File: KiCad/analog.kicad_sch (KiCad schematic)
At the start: 25 parts, among them J1 Conn_01x02, U1 LM1117T-3.3, U2 LM2596T-5

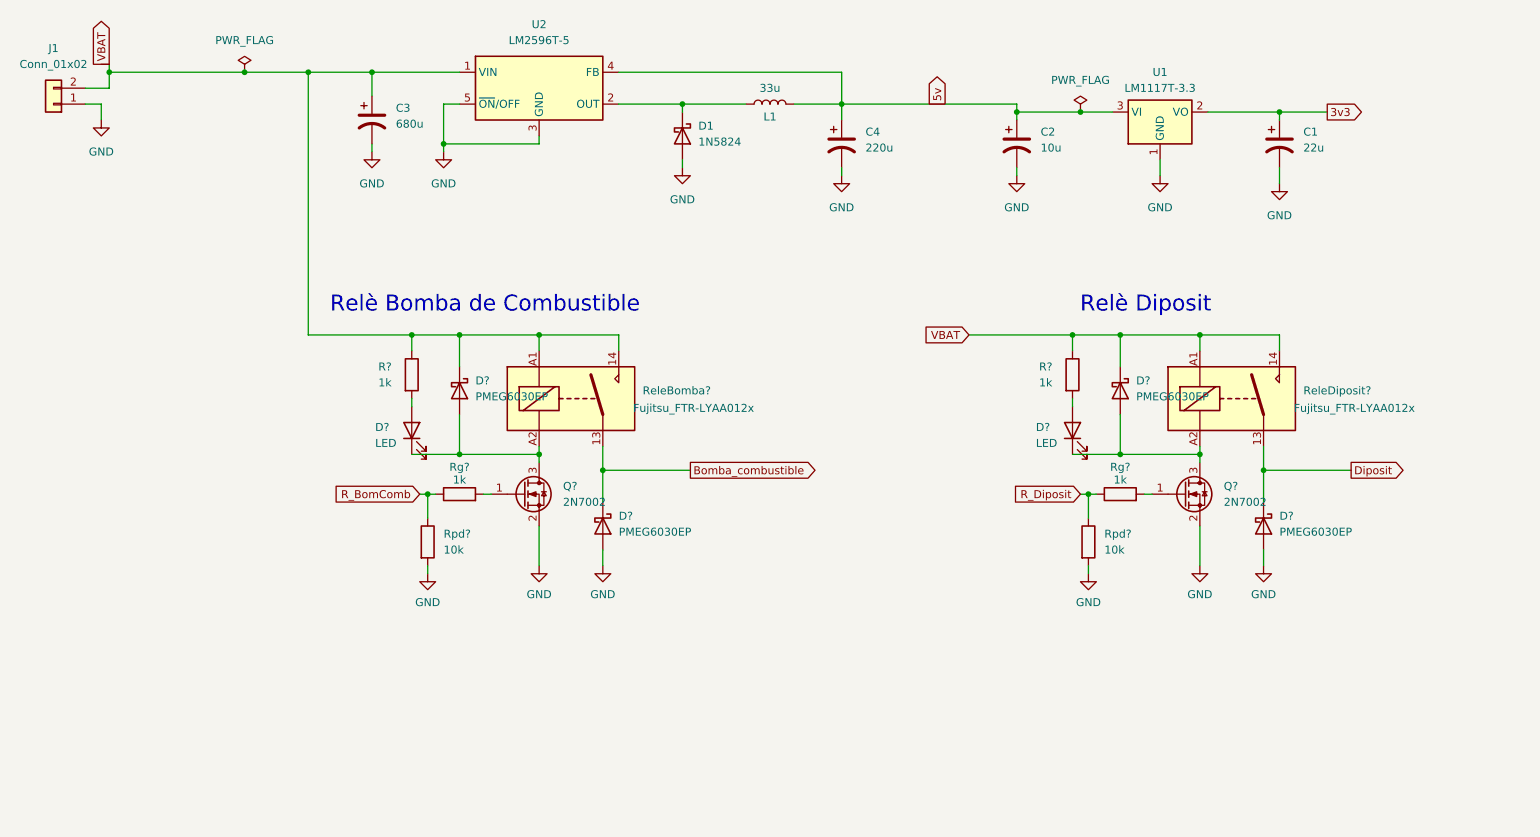
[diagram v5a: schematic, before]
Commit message: Sheets nombrades amb titol, i part del supply millorada
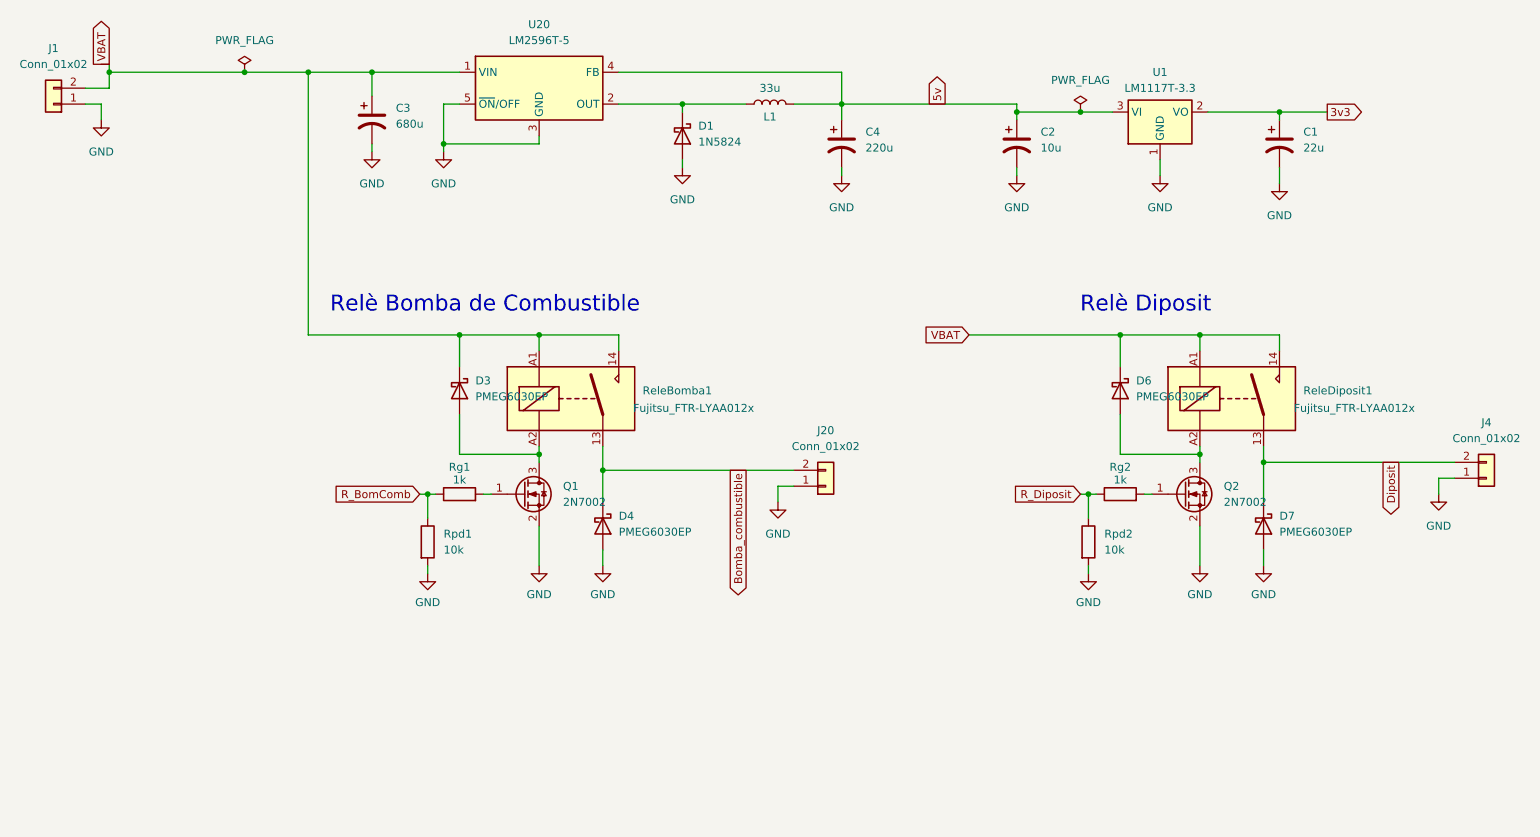
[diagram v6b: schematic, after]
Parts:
- removed D? (x2): LED, LED_SMD:LED_0805_2012Metric, symbol Device:LED
- removed R? (x2): 1k, Resistor_SMD:R_1206_3216Metric, symbol Device:R
- added J20, J4: Conn_01x02, symbol Connector_Generic:Conn_01x02
- gave numbers to parts that had none: 12
- renumbered U2 to U20
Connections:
- net Bomba_combustible: now also J20.2 (Pin_2)
- net Diposit: now also J4.2 (Pin_2)
- net GND: now also J20.1 (Pin_1), J4.1 (Pin_1)
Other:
- title: (none) -> Power Supply & Relés

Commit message: sheets editades
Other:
- note added: "Regulador Buck, mes LDO i Relès per a la bomba i el diposit."
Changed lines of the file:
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@@
+		)
+	)
+	(text "Regulador Buck, mes LDO i Relès per a la bomba i el diposit."
+		(exclude_from_sim no)
+		(at 209.296 168.402 0)
+		(effects
+			(font
+				(size 1.27 1.27)
+			)
 		)
 	)

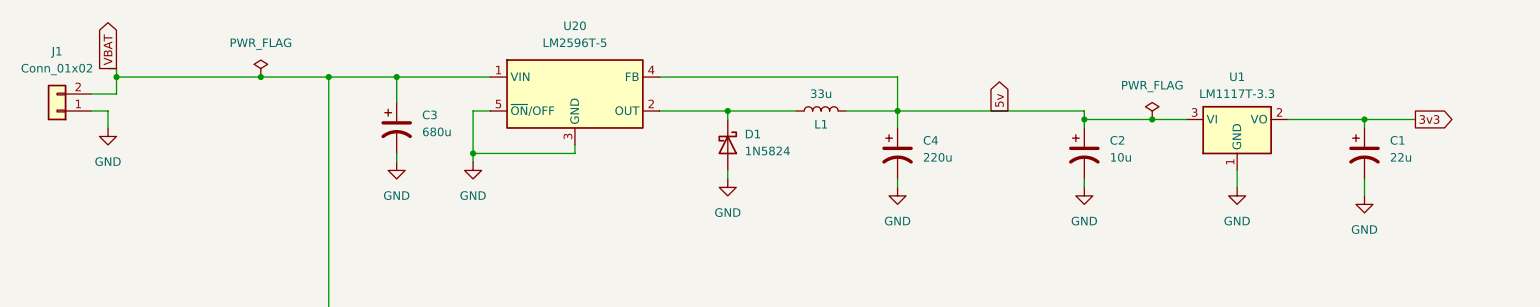
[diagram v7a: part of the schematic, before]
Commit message: Totes les footprints seleccionades, part de potencia, placement realitzat
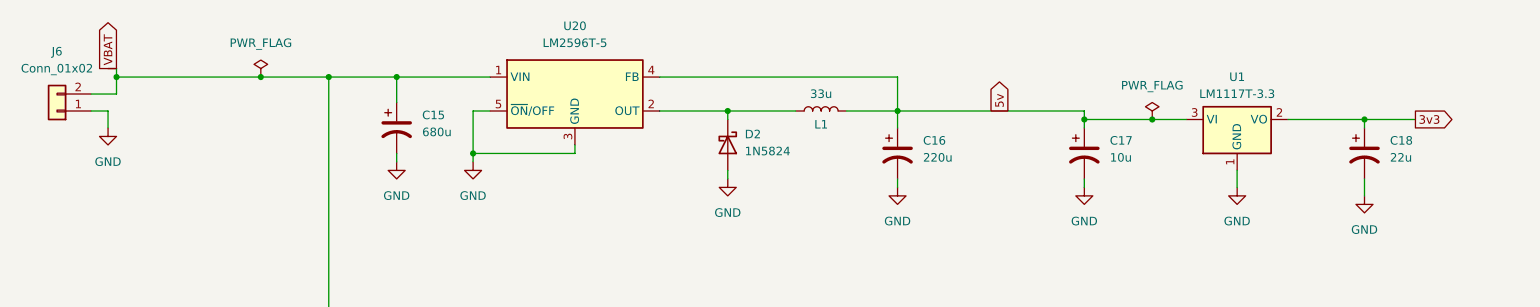
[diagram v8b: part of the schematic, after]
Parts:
- C15: renamed from C3; footprint (none) -> Capacitor_SMD:CP_Elec_10x10
- C16: renamed from C4; footprint (none) -> Capacitor_SMD:CP_Elec_10x10
- C17: renamed from C2; footprint (none) -> Capacitor_Tantalum_SMD:CP_EIA-3528-12_Kemet-T
- C18: renamed from C1; footprint (none) -> Capacitor_Tantalum_SMD:CP_EIA-3216-12_Kemet-S
- J20, J4: footprint (none) -> Connector_PinHeader_2.54mm:PinHeader_1x02_P2.54mm_Vertical
- J6: renamed from J1; footprint (none) -> Connector_PinHeader_2.54mm:PinHeader_1x02_P2.54mm_Vertical
- L1: footprint (none) -> Inductor_SMD:L_1206_3216Metric
- renumbered D1 to D2
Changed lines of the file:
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@@
 		(dnp no)
 		(fields_autoplaced yes)
-		(property "Reference" "C?"
+		(property "Reference" "C15"
 			(at 78.74 55.2449 0)
 			(effects
@@
 			)
 		)
-		(property "Footprint" ""
+		(property "Footprint" "Capacitor_SMD:CP_Elec_10x10"
 			(at 74.93 57.15 0)
 			(effects
@@
 			(project "Combustible_projecte"
 				(path "/c989196d-f442-462e-ad13-2ff17993bc1b/9cc53e55-b115-43a5-9a22-06f8c68fe0c0"
-					(reference "C?")
+					(reference "C15")
 					(unit 1)
 				)
@@
 		(dnp no)
 		(fields_autoplaced yes)
-		(property "Reference" "#PWR?"
+		(property "Reference" "#PWR0116"
 			(at 149.86 72.39 0)
 			(effects
@@
 			(project "Combustible_projecte"
 				(path "/c989196d-f442-462e-ad13-2ff17993bc1b/9cc53e55-b115-43a5-9a22-06f8c68fe0c0"
-					(reference "#PWR?")
+					(reference "#PWR0116")
 					(unit 1)
 				)
@@
 		(dnp no)
 		(fields_autoplaced yes)
-		(property "Reference" "C?"
+		(property "Reference" "C18"
 			(at 223.52 59.0549 0)
 			(effects
@@
 			)
 		)
-		(property "Footprint" ""
+		(property "Footprint" "Capacitor_Tantalum_SMD:CP_EIA-3216-12_Kemet-S"
 			(at 219.71 60.96 0)
 			(effects
@@
 			(project "Combustible_projecte"
 				(path "/c989196d-f442-462e-ad13-2ff17993bc1b/9cc53e55-b115-43a5-9a22-06f8c68fe0c0"
-					(reference "C?")
+					(reference "C18")
 					(unit 1)
 				)
@@
 		(dnp no)
 		(fields_autoplaced yes)
-		(property "Reference" "#PWR?"
+		(property "Reference" "#PWR0114"
 			(at 200.66 72.39 0)
 			(effects
@@
 			(project "Combustible_projecte"
 				(path "/c989196d-f442-462e-ad13-2ff17993bc1b/9cc53e55-b115-43a5-9a22-06f8c68fe0c0"
-					(reference "#PWR?")
+					(reference "#PWR0114")
 					(unit 1)
 				)
@@
 		(dnp no)
 		(fields_autoplaced yes)
-		(property "Reference" "C?"
+		(property "Reference" "C17"
 			(at 181.61 59.0549 0)
 			(effects
@@
 			)
 		)
-		(property "Footprint" ""
+		(property "Footprint" "Capacitor_Tantalum_SMD:CP_EIA-3528-12_Kemet-T"
 			(at 177.8 60.96 0)
 			(effects
@@
 			(project "Combustible_projecte"
 				(path "/c989196d-f442-462e-ad13-2ff17993bc1b/9cc53e55-b115-43a5-9a22-06f8c68fe0c0"
-					(reference "C?")
+					(reference "C17")
 					(unit 1)
 				)
@@
 		(dnp no)
 		(fields_autoplaced yes)
-		(property "Reference" "#PWR?"
+		(property "Reference" "#PWR0117"
 			(at 124.46 71.12 0)
 			(effects
@@
 			(project "Combustible_projecte"
 				(path "/c989196d-f442-462e-ad13-2ff17993bc1b/9cc53e55-b115-43a5-9a22-06f8c68fe0c0"
-					(reference "#PWR?")
+					(reference "#PWR0117")
 					(unit 1)
 				)
@@
 		(dnp no)
 		(fields_autoplaced yes)
-		(property "Reference" "D?"
+		(property "Reference" "D2"
 			(at 127 58.1024 90)
 			(effects
@@
 			(project "Combustible_projecte"
 				(path "/c989196d-f442-462e-ad13-2ff17993bc1b/9cc53e55-b115-43a5-9a22-06f8c68fe0c0"
-					(reference "D?")
+					(reference "D2")
 					(unit 1)
 				)
@@
 			)
 		)
-		(property "Footprint" ""
+		(property "Footprint" "Connector_PinHeader_2.54mm:PinHeader_1x02_P2.54mm_Vertical"
 			(at 147.32 115.57 0)
 			(effects
@@
 		(dnp no)
 		(fields_autoplaced yes)
-		(property "Reference" "#PWR?"
+		(property "Reference" "#PWR0111"
 			(at 74.93 68.58 0)
 			(effects
@@
 			(project "Combustible_projecte"
 				(path "/c989196d-f442-462e-ad13-2ff17993bc1b/9cc53e55-b115-43a5-9a22-06f8c68fe0c0"
-					(reference "#PWR?")
+					(reference "#PWR0111")
 					(unit 1)
 				)
@@
 		(dnp no)
 		(fields_autoplaced yes)
-		(property "Reference" "#PWR?"
+		(property "Reference" "#PWR0110"
 			(at 86.36 68.58 0)
 			(effects
@@
 			(project "Combustible_projecte"
 				(path "/c989196d-f442-462e-ad13-2ff17993bc1b/9cc53e55-b115-43a5-9a22-06f8c68fe0c0"
-					(reference "#PWR?")
+					(reference "#PWR0110")
 					(unit 1)
 				)
@@
 		(dnp no)
 		(fields_autoplaced yes)
-		(property "Reference" "C?"
+		(property "Reference" "C16"
 			(at 153.67 59.0549 0)
 			(effects
@@
 			)
 		)
-		(property "Footprint" ""
+		(property "Footprint" "Capacitor_SMD:CP_Elec_10x10"
 			(at 149.86 60.96 0)
 			(effects
@@
 			(project "Combustible_projecte"
 				(path "/c989196d-f442-462e-ad13-2ff17993bc1b/9cc53e55-b115-43a5-9a22-06f8c68fe0c0"
-					(reference "C?")
+					(reference "C16")
 					(unit 1)
 				)
@@
 		(dnp no)
 		(fields_autoplaced yes)
-		(property "Reference" "#PWR?"
+		(property "Reference" "#PWR0113"
 			(at 177.8 72.39 0)
 			(effects
@@
 			(project "Combustible_projecte"
 				(path "/c989196d-f442-462e-ad13-2ff17993bc1b/9cc53e55-b115-43a5-9a22-06f8c68fe0c0"
-					(reference "#PWR?")
+					(reference "#PWR0113")
 					(unit 1)
 				)
@@
 			)
 		)
-		(property "Footprint" ""
+		(property "Footprint" "Connector_PinHeader_2.54mm:PinHeader_1x02_P2.54mm_Vertical"
 			(at 252.73 114.3 0)
 			(effects
@@
 		(dnp no)
 		(fields_autoplaced yes)
-		(property "Reference" "#PWR?"
+		(property "Reference" "#PWR0115"
 			(at 219.71 73.66 0)
 			(effects
@@
 			(project "Combustible_projecte"
 				(path "/c989196d-f442-462e-ad13-2ff17993bc1b/9cc53e55-b115-43a5-9a22-06f8c68fe0c0"
-					(reference "#PWR?")
+					(reference "#PWR0115")
 					(unit 1)
 				)
@@
 		(dnp no)
 		(fields_autoplaced yes)
-		(property "Reference" "J?"
+		(property "Reference" "J6"
 			(at 24.13 45.72 0)
 			(effects
@@
 			)
 		)
-		(property "Footprint" ""
+		(property "Footprint" "Connector_PinHeader_2.54mm:PinHeader_1x02_P2.54mm_Vertical"
 			(at 24.13 54.61 0)
 			(effects
@@
 			(project "Combustible_projecte"
 				(path "/c989196d-f442-462e-ad13-2ff17993bc1b/9cc53e55-b115-43a5-9a22-06f8c68fe0c0"
-					(reference "J?")
+					(reference "J6")
 					(unit 1)
 				)
@@
 		(dnp no)
 		(fields_autoplaced yes)
-		(property "Reference" "#PWR?"
+		(property "Reference" "#PWR0112"
 			(at 31.75 63.5 0)
 			(effects
@@
 			(project "Combustible_projecte"
 				(path "/c989196d-f442-462e-ad13-2ff17993bc1b/9cc53e55-b115-43a5-9a22-06f8c68fe0c0"
-					(reference "#PWR?")
+					(reference "#PWR0112")
 					(unit 1)
 				)
@@
 		(on_board yes)
 		(dnp no)
-		(property "Reference" "L?"
+		(property "Reference" "L1"
 			(at 138.43 56.642 90)
 			(effects
@@
 			)
 		)
-		(property "Footprint" ""
+		(property "Footprint" "Inductor_SMD:L_1206_3216Metric"
 			(at 138.43 54.61 0)
 			(effects
@@
 			(project "Combustible_projecte"
 				(path "/c989196d-f442-462e-ad13-2ff17993bc1b/9cc53e55-b115-43a5-9a22-06f8c68fe0c0"
-					(reference "L?")
-					(unit 1)
-				)
+					(reference "L1")
+					(unit 1)
+				)
